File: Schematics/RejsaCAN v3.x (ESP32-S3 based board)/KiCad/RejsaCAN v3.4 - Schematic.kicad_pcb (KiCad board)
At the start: 2 copper layers, 31.5 x 49.5 mm, 69 parts, among them Q1 SS8050, U1 ESP32-S3-WROOM-1(N16R8), U2 SN65HVD230DR, U3 ME2807A33M3G, U4 LMR14006XDDCR, U5 MT9700

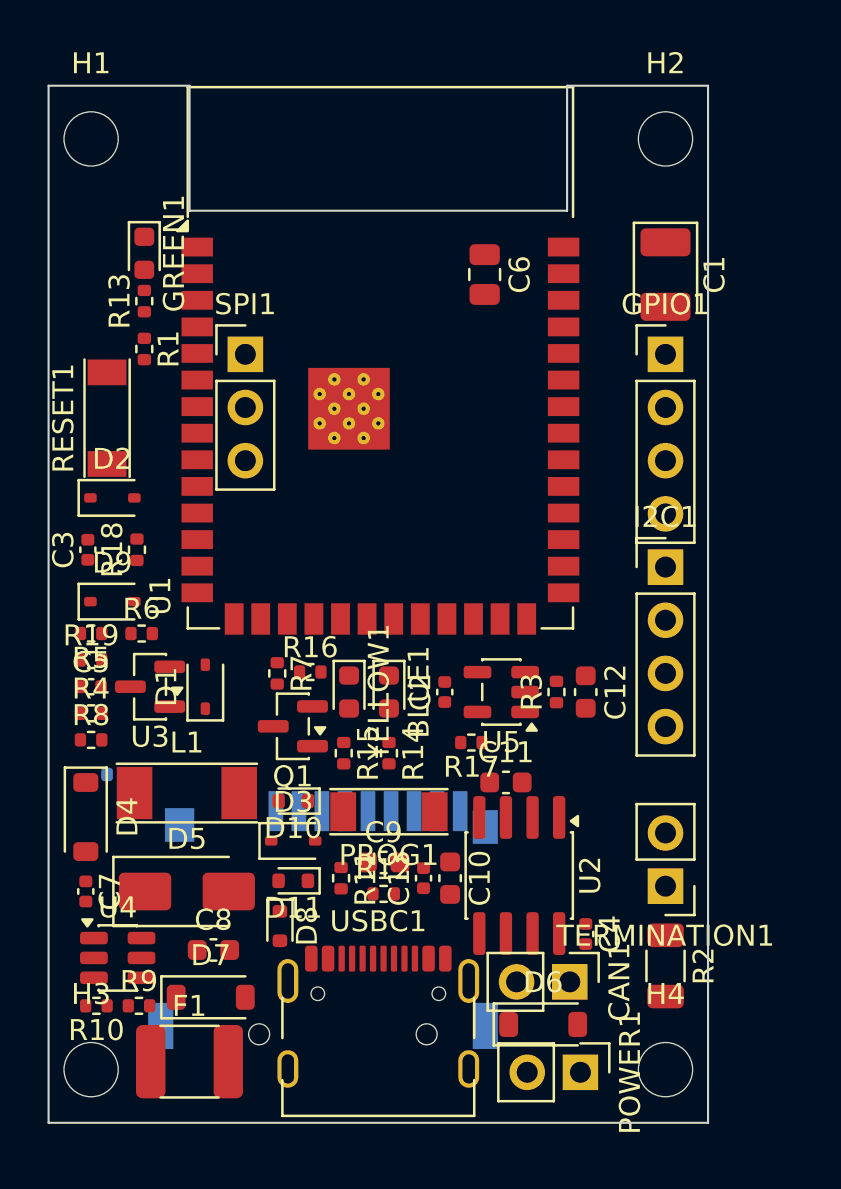
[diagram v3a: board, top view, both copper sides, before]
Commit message: Route the v3.4 board: 555 tracks, 116 vias, ground pours both layers
DRC is clean of every electrical class: no shorts, no clearance violations, no
mask bridges, no dangling ends, no hole-spacing or annular problems, and zero
schematic-parity errors. 16 connections remain open (see below).

The autorouter is driven with settings taken from Freerouting's own docs rather
than guessed, which changed the outcome substantially:

  --gui.enabled=false             the NullPointerException that fired on every
                                  previous run was in ConductionArea's *paint*
                                  path, not the router; headless never hits it
  --router.optimizer.enabled=false  Freerouting keeps no best-seen board, so the
                                  optimizer's worse result simply overwrote the
                                  good one (4 unrouted became 7)
  --router.layers.preferred_direction_horizontal=true,false
                                  horizontal on top, vertical on bottom -- the
                                  main completion lever on a 2-layer board

Result went from 32 clearance violations to 0, and copper from 869mm to 985mm.

The finishing pass (joining what the router left, grounding stranded pads) is
rewritten around KiCad's own connectivity graph -- GetConnectedItems tells us
which pads are genuinely cut off from the main ground, instead of inferring it
from proximity. Four bugs in the previous geometry are fixed:

  - obstacles are now filtered by layer, so an F.Cu route is no longer blocked
    by pads that only exist on B.Cu (this alone was why connections reported
    "no clean path")
  - vias are checked as vias: copper clearance on BOTH layers plus hole-to-hole
    spacing. Checking only the copper stub is what produced 12 shorts and 12
    co-located holes
  - clearance is per-obstacle -- 0.35mm near the battery nets, 0.15mm elsewhere.
    A blanket strictest-class value was wrong in both directions
  - the endpoin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
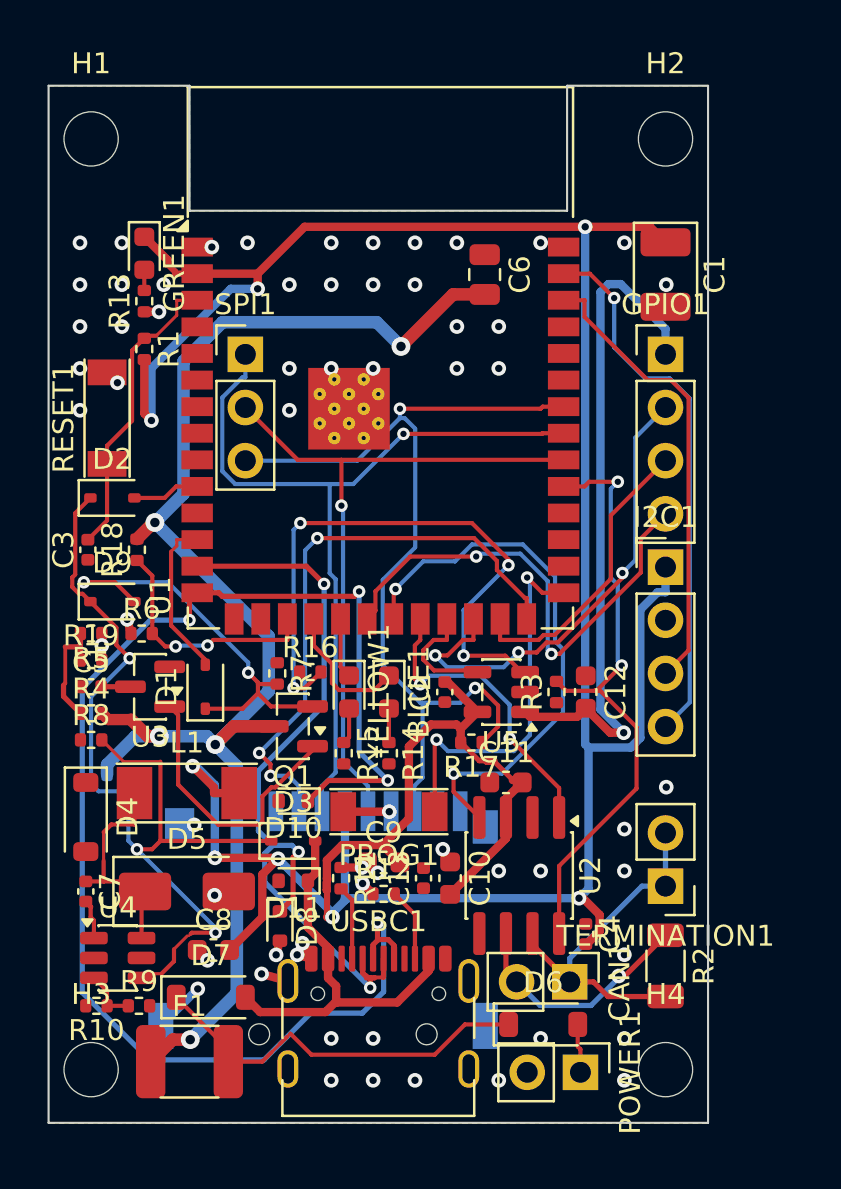
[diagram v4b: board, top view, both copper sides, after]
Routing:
- net 3V3: track 0.00 -> 152.9 mm, vias 0 -> 8
- net VCC: track 0.00 -> 70.5 mm, vias 0 -> 5
- net USB_D+: track 0.00 -> 68.0 mm, vias 0 -> 4
- net Net-(D2-K): track 0.00 -> 45.6 mm, vias 0 -> 3
- net MTDI: track 0.00 -> 43.7 mm, vias 0 -> 2
- net MTDO: track 0.00 -> 39.7 mm, vias 0 -> 1
- net USB_D-: track 0.00 -> 37.3 mm, vias 0 -> 3
- net MTCK: track 0.00 -> 33.5 mm, vias 0 -> 1
- net 3V3_SWITCHED: track 0.00 -> 32.3 mm, vias 0 -> 1
- net CAN_RS: track 0.00 -> 29.7 mm, vias 0 -> 2
- net Net-(U5-SET): track 0.00 -> 29.1 mm, vias 0 -> 4
- net SD_CARD: track 0.00 -> 27.9 mm, vias 0 -> 3
- net CAN_RX: track 0.00 -> 26.3 mm, vias 0 -> 2
- net SDA: track 0.00 -> 26.0 mm, vias 0 -> 1
- net GPIO12: track 0.00 -> 23.7 mm, vias 0 -> 2
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- added copper zone on B.Cu, net GND
- added copper zone on F.Cu, net GND
